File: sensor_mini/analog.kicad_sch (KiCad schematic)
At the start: 37 parts, among them J2 Conn_01x02_Female-Connector, J3 Conn_01x02_Female-Connector, J4 Conn_01x02_Female-Connector, J5 Conn_01x02_Female-Connector, U4 TLV9002IDR

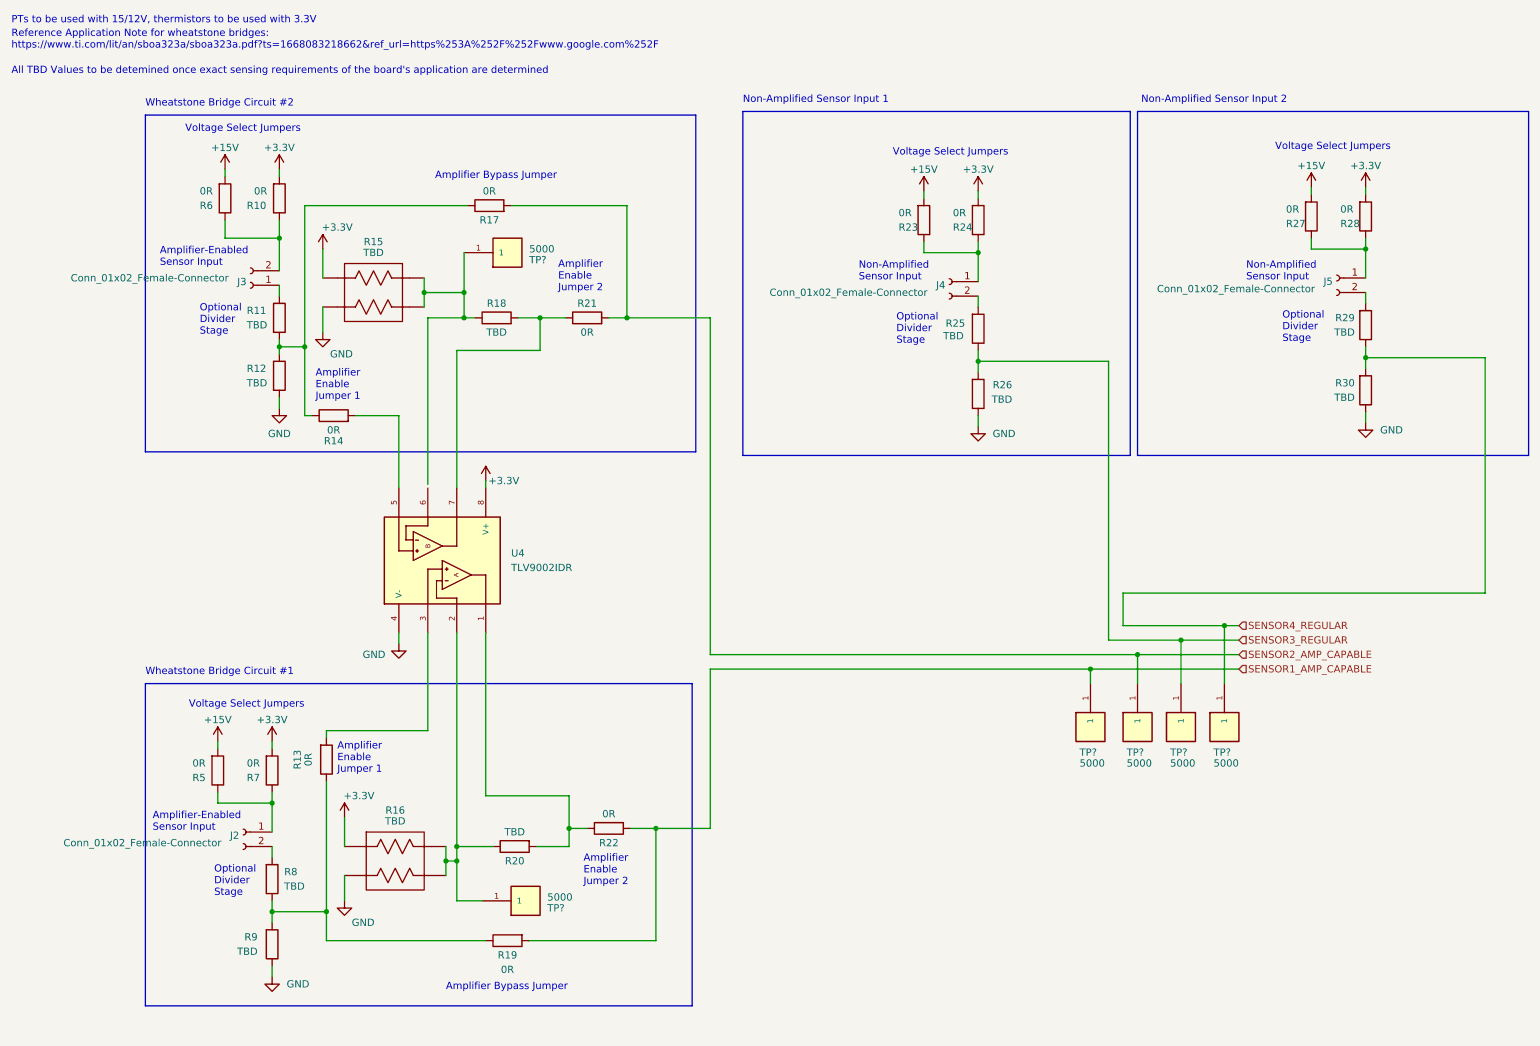
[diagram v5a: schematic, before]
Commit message: Clean up the festering cesspool that was the minisensor folder
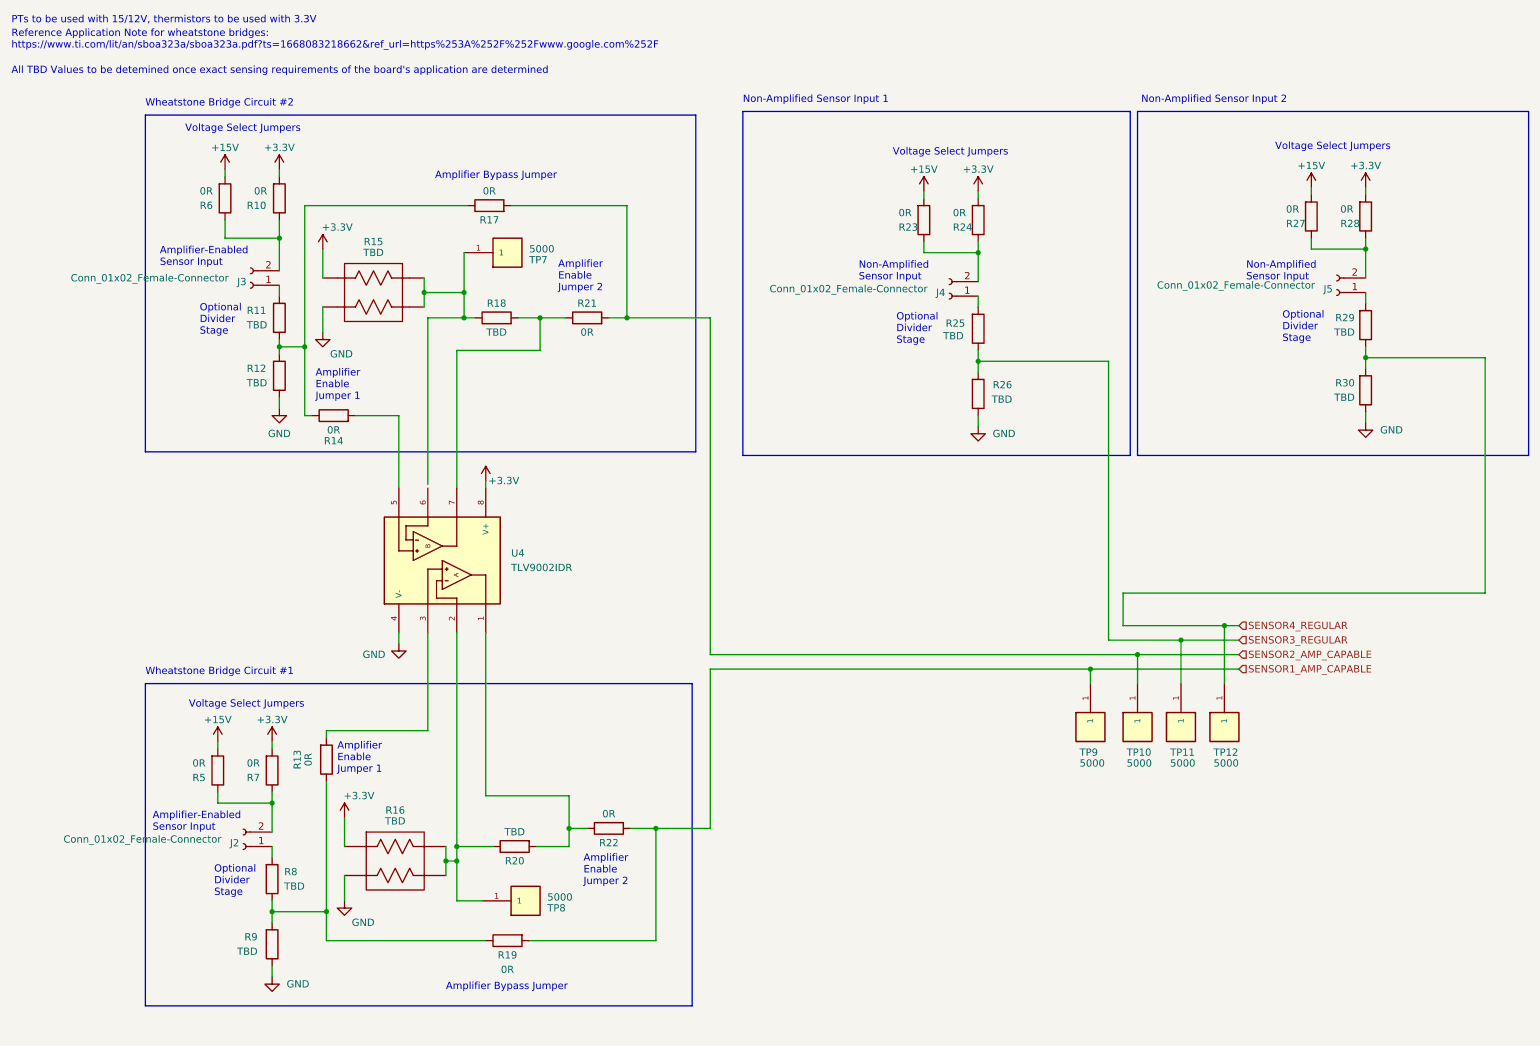
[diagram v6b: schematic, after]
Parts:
- removed J2, J4, J5: Conn_01x02_Female-Connector, Connector_JST:JST_PH_S2B-PH-K_1x02_P2.00mm_Horizontal, symbol sensors-rescue:Conn_01x02_Female-Connector
- added J2, J4, J5: Conn_01x02_Female-Connector, Connector_JST:JST_PH_S2B-PH-K_1x02_P2.00mm_Horizontal, symbol Connector:Conn_01x02_Female
- J3: symbol sensors-rescue:Conn_01x02_Female-Connector -> Connector:Conn_01x02_Female
- R15, R16: symbol ACA_Percision_Vishay:2_RES_ARRAY -> CANHW:ACAS06
- gave numbers to parts that had none: 6
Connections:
- net at R27.1, R28.1: now also J5.2 (Pin_2)
- net at R29.2: now also J5.1 (Pin_1)
- net at R23.1, R24.1: now also J4.2 (Pin_2)
- net at R25.2: now also J4.1 (Pin_1)
- net at R5.1, R7.1: now also J2.2 (Pin_2)
- net at R8.2: now also J2.1 (Pin_1)
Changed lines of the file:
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@@
     (pin "2")
   )
-  (symbol (lib_id "sensors-rescue:Conn_01x02_Female-Connector") (at 246.38 59.055 0) (mirror y) (unit 1)
-    (in_bom yes) (on_board yes)
-    (property "Reference" "J5" (id 0) (at 245.6942 59.6646 0)
-      (effects (font (size 1.27 1.27)) (justify left))
-    )
-    (property "Value" "Conn_01x02_Female-Connector" (id 1) (at 242.57 60.96 0)
-      (effects (font (size 1.27 1.27)) (justify left))
-    )
-    (property "Footprint" "Connector_JST:JST_PH_S2B-PH-K_1x02_P2.00mm_Horizontal" (id 2) (at 246.38 59.055 0)
-      (effects (font (size 1.27 1.27)) hide)
-    )
-    (property "Datasheet" "~" (id 3) (at 246.38 59.055 0)
+  (symbol (lib_id "Connector:Conn_01x02_Female") (at 54.61 158.75 180) (unit 1)
+    (in_bom yes) (on_board yes)
+    (property "Reference" "J2" (id 0) (at 53.9242 158.1404 0)
+      (effects (font (size 1.27 1.27)) (justify left))
+    )
+    (property "Value" "Conn_01x02_Female-Connector" (id 1) (at 50.8 157.48 0)
+      (effects (font (size 1.27 1.27)) (justify left))
+    )
+    (property "Footprint" "Connector_JST:JST_PH_S2B-PH-K_1x02_P2.00mm_Horizontal" (id 2) (at 54.61 158.75 0)
+      (effects (font (size 1.27 1.27)) hide)
+    )
+    (property "Datasheet" "~" (id 3) (at 54.61 158.75 0)
       (effects (font (size 1.27 1.27)) hide)
     )
@@
     (pin "2")
   )
-  (symbol (lib_id "sensors-rescue:Conn_01x02_Female-Connector") (at 178.435 59.69 0) (mirror y) (unit 1)
-    (in_bom yes) (on_board yes)
-    (property "Reference" "J4" (id 0) (at 177.7492 60.2996 0)
-      (effects (font (size 1.27 1.27)) (justify left))
-    )
-    (property "Value" "Conn_01x02_Female-Connector" (id 1) (at 174.625 61.595 0)
-      (effects (font (size 1.27 1.27)) (justify left))
-    )
-    (property "Footprint" "Connector_JST:JST_PH_S2B-PH-K_1x02_P2.00mm_Horizontal" (id 2) (at 178.435 59.69 0)
-      (effects (font (size 1.27 1.27)) hide)
-    )
-    (property "Datasheet" "~" (id 3) (at 178.435 59.69 0)
-      (effects (font (size 1.27 1.27)) hide)
-    )
-    (pin "1")
-    (pin "2")
-  )
   (symbol (lib_id "Device:R") (at 60.96 76.2 0) (unit 1)
     (in_bom yes) (on_board yes)
@@
   (symbol (lib_id "Keysight_5000_testpoints:5000") (at 226.695 137.795 270) (unit 1)
     (in_bom yes) (on_board yes)
-    (property "Reference" "TP?" (id 0) (at 224.79 142.24 90)
+    (property "Reference" "TP12" (id 0) (at 224.79 142.24 90)
       (effects (font (size 1.27 1.27)) (justify left))
     )
@@
   (symbol (lib_id "Keysight_5000_testpoints:5000") (at 104.14 168.275 0) (unit 1)
     (in_bom yes) (on_board yes)
-    (property "Reference" "TP?" (id 0) (at 107.95 169.545 0)
+    (property "Reference" "TP8" (id 0) (at 107.95 169.545 0)
       (effects (font (size 1.27 1.27)) (justify left))
     )
@@
     (pin "1")
   )
-  (symbol (lib_id "sensors-rescue:Conn_01x02_Female-Connector") (at 55.88 60.325 180) (unit 1)
+  (symbol (lib_id "Connector:Conn_01x02_Female") (at 55.88 60.325 180) (unit 1)
     (in_bom yes) (on_board yes)
     (property "Reference" "J3" (id 0) (at 55.1942 59.7154 0)
@@
   (symbol (lib_id "Keysight_5000_testpoints:5000") (at 219.075 137.795 270) (unit 1)
     (in_bom yes) (on_board yes)
-    (property "Reference" "TP?" (id 0) (at 217.17 142.24 90)
+    (property "Reference" "TP11" (id 0) (at 217.17 142.24 90)
       (effects (font (size 1.27 1.27)) (justify left))
     )
@@
     )
     (property "Datasheet" "~" (id 3) (at 70.485 83.185 0)
-      (effects (font (size 1.27 1.27)) hide)
-    )
-    (pin "1")
-    (pin "2")
-  )
-  (symbol (lib_id "sensors-rescue:Conn_01x02_Female-Connector") (at 54.61 156.21 0) (mirror y) (unit 1)
-    (in_bom yes) (on_board yes)
-    (property "Reference" "J2" (id 0) (at 53.9242 156.8196 0)
-      (effects (font (size 1.27 1.27)) (justify left))
-    )
-    (property "Value" "Conn_01x02_Female-Connector" (id 1) (at 50.8 158.115 0)
-      (effects (font (size 1.27 1.27)) (justify left))
-    )
-    (property "Footprint" "Connector_JST:JST_PH_S2B-PH-K_1x02_P2.00mm_Horizontal" (id 2) (at 54.61 156.21 0)
-      (effects (font (size 1.27 1.27)) hide)
-    )
-    (property "Datasheet" "~" (id 3) (at 54.61 156.21 0)
       (effects (font (size 1.27 1.27)) hide)
     )
@@
     (pin "2")
   )
+  (symbol (lib_id "Connector:Conn_01x02_Female") (at 246.38 61.595 180) (unit 1)
+    (in_bom yes) (on_board yes)
+    (property "Reference" "J5" (id 0) (at 245.6942 60.9854 0)
+      (effects (font (size 1.27 1.27)) (justify left))
+    )
+    (property "Value" "Conn_01x02_Female-Connector" (id 1) (at 242.57 60.325 0)
+      (effects (font (size 1.27 1.27)) (justify left))
+    )
+    (property "Footprint" "Connector_JST:JST_PH_S2B-PH-K_1x02_P2.00mm_Horizontal" (id 2) (at 246.38 61.595 0)
+      (effects (font (size 1.27 1.27)) hide)
+    )
+    (property "Datasheet" "~" (id 3) (at 246.38 61.595 0)
+      (effects (font (size 1.27 1.27)) hide)
+    )
+    (pin "1")
+    (pin "2")
+  )
   (symbol (lib_id "Keysight_5000_testpoints:5000") (at 211.455 137.795 270) (unit 1)
     (in_bom yes) (on_board yes)
-    (property "Reference" "TP?" (id 0) (at 209.55 142.24 90)
+    (property "Reference" "TP10" (id 0) (at 209.55 142.24 90)
       (effects (font (size 1.27 1.27)) (justify left))
     )
@@
     (pin "2")
   )
-  (symbol (lib_id "ACA_Percision_Vishay:2_RES_ARRAY") (at 77.47 61.595 0) (unit 1)
+  (symbol (lib_id "CANHW:ACAS06") (at 77.47 61.595 0) (unit 1)
     (in_bom yes) (on_board yes)
     (property "Reference" "R15" (id 0) (at 77.47 52.705 0))
@@
       (effects (font (size 1.27 1.27)) hide)
     )
-    (property "Datasheet" "https://www.vishay.com/docs/28770/acasat.pdf" (id 3) (at 80.645 72.39 0)
+    (property "Datasheet" "https://www.vishay.com/docs/28770/acasat.pdf" (id 3) (at 78.74 69.215 0)
       (effects (font (size 1.27 1.27)) hide)
     )
@@
     (pin "2")
   )
+  (symbol (lib_id "Connector:Conn_01x02_Female") (at 178.435 62.23 180) (unit 1)
+    (in_bom yes) (on_board yes)
+    (property "Reference" "J4" (id 0) (at 177.7492 61.6204 0)
+      (effects (font (size 1.27 1.27)) (justify left))
+    )
+    (property "Value" "Conn_01x02_Female-Connector" (id 1) (at 174.625 60.96 0)
+      (effects (font (size 1.27 1.27)) (justify left))
+    )
+    (property "Footprint" "Connector_JST:JST_PH_S2B-PH-K_1x02_P2.00mm_Horizontal" (id 2) (at 178.435 62.23 0)
+      (effects (font (size 1.27 1.27)) hide)
+    )
+    (property "Datasheet" "~" (id 3) (at 178.435 62.23 0)
+      (effects (font (size 1.27 1.27)) hide)
+    )
+    (pin "1")
+    (pin "2")
+  )
   (symbol (lib_id "Device:R") (at 100.965 175.26 90) (mirror x) (unit 1)
     (in_bom yes) (on_board yes)
@@
     (pin "2")
   )
-  (symbol (lib_id "ACA_Percision_Vishay:2_RES_ARRAY") (at 81.28 161.29 0) (unit 1)
+  (symbol (lib_id "CANHW:ACAS06") (at 81.28 161.29 0) (unit 1)
     (in_bom yes) (on_board yes)
     (property "Reference" "R16" (id 0) (at 81.28 152.4 0))
@@
       (effects (font (size 1.27 1.27)) hide)
     )
-    (property "Datasheet" "https://www.vishay.com/docs/28770/acasat.pdf" (id 3) (at 84.455 172.085 0)
+    (property "Datasheet" "https://www.vishay.com/docs/28770/acasat.pdf" (id 3) (at 82.55 168.91 0)
       (effects (font (size 1.27 1.27)) hide)
     )
@@
   (symbol (lib_id "Keysight_5000_testpoints:5000") (at 203.2 137.795 270) (unit 1)
     (in_bom yes) (on_board yes)
-    (property "Reference" "TP?" (id 0) (at 201.295 142.24 90)
+    (property "Reference" "TP9" (id 0) (at 201.295 142.24 90)
       (effects (font (size 1.27 1.27)) (justify left))
     )
@@
   (symbol (lib_id "Keysight_5000_testpoints:5000") (at 100.965 54.61 0) (unit 1)
     (in_bom yes) (on_board yes)
-    (property "Reference" "TP?" (id 0) (at 104.775 55.88 0)
-      (effects (font (size 1.27 1.27)) (justify left))
-    )
+    (property "Reference" "TP7" (id 0) (at 104.775 55.88 0)
+      (effects (font (size 1.27 1.27)) (justify left))
+    )

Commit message: Clean up schematic, add trims on bridge legs
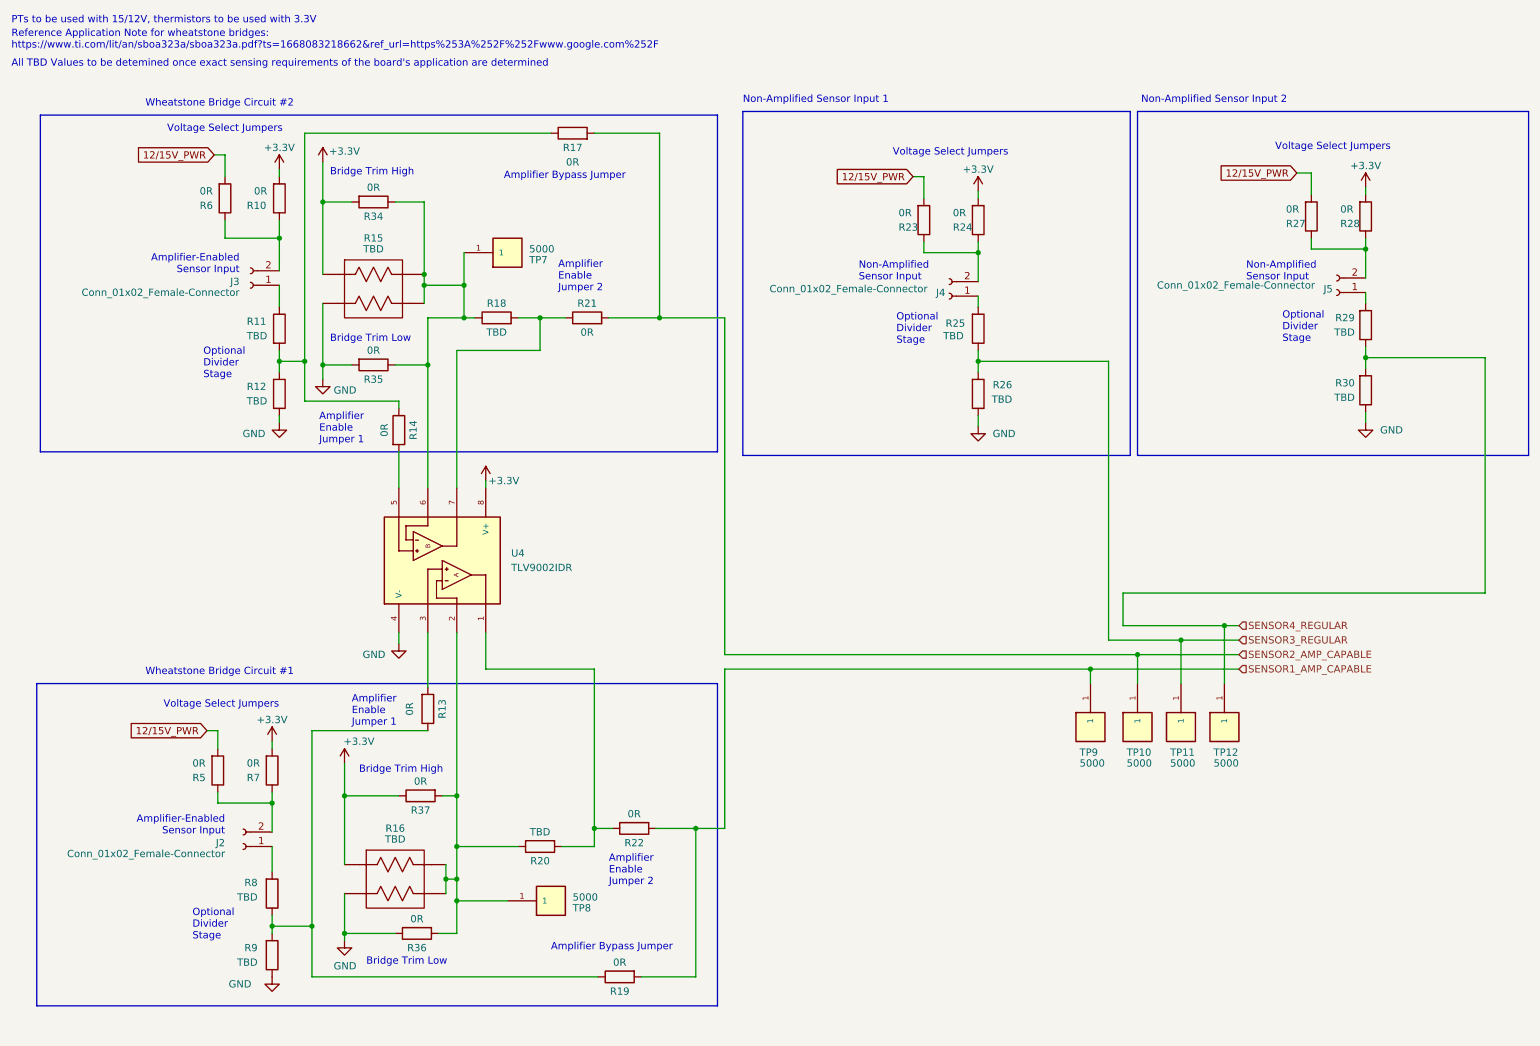
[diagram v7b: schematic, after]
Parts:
- added R34, R35, R36, R37: 0R, symbol Device:R
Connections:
- net +3V3: now also R34.2, R37.1
- net GND: now also R35.2, R36.1
- net at R15., R18.1, TP7.1: now also U4.6, R34.1, R35.1
- net at R16., R20.1, TP8.1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: now also R36.2, R37.2
- net +15V renamed 12/15V_PWR
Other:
- note added: "Bridge Trim High"
- note added: "Bridge Trim Low"
- moved on the sheet: R11, R12, R13, R14, R15, R16, R17, R19, R20, R22, R8, R9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
